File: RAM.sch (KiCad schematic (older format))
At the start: 47 parts, among them U2 AS4C256M16D3LC-12BCN, U3 AS4C256M16D3LC-12BCN

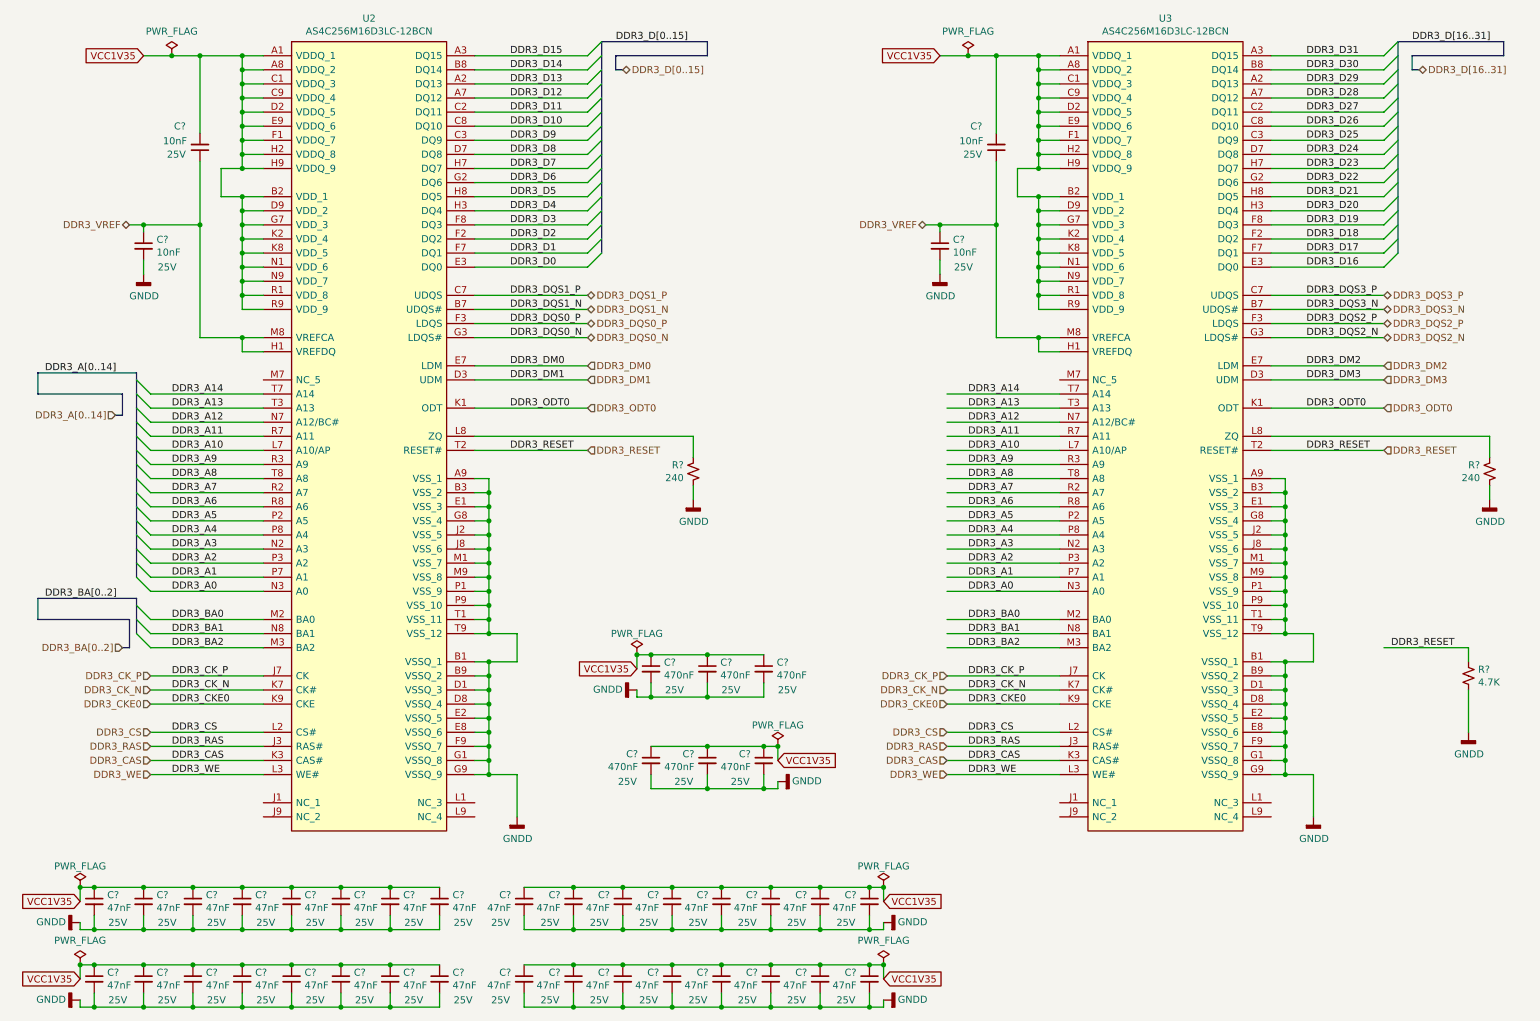
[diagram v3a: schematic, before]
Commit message: PCB created and schematics annotated High speed connections added to the BTB
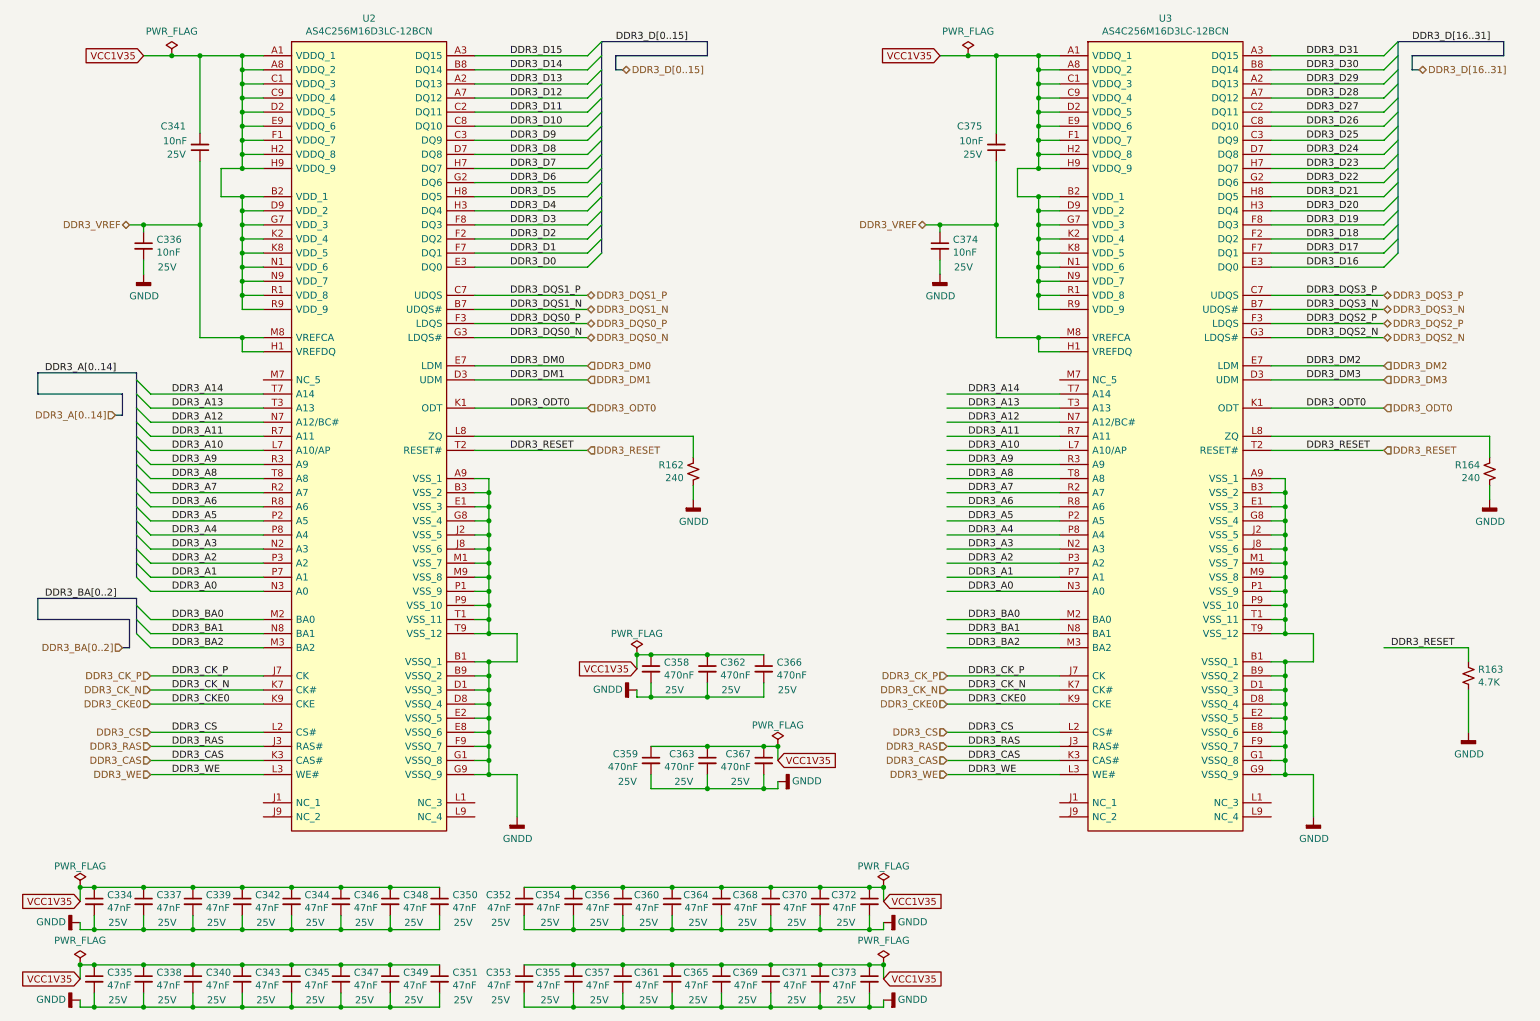
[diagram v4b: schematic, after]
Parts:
- gave numbers to parts that had none: 45

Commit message: Corrected PCB import errors
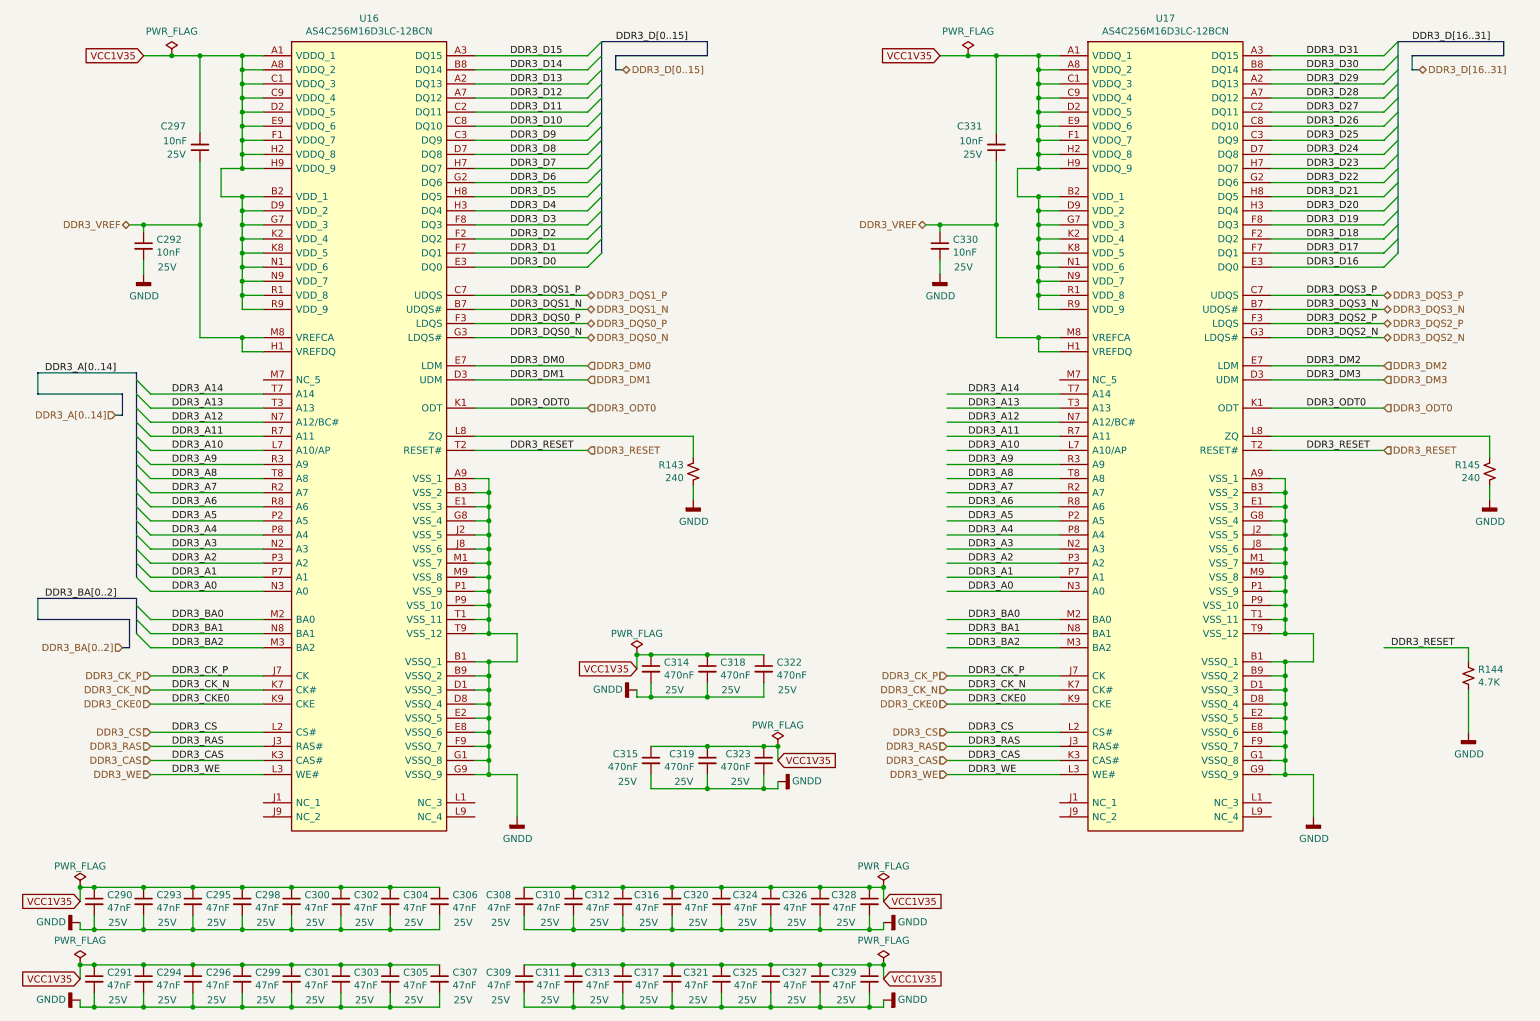
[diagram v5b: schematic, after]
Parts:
- renumbered C334 to C290, C335 to C291, C336 to C292, C337 to C293, C338 to C294, C339 to C295, C340 to C296, C341 to C297, C342 to C298, C343 to C299, C344 to C300, C345 to C301, C346 to C302, C347 to C303, C348 to C304, C349 to C305, C350 to C306, C351 to C307, C352 to C308, C353 to C309, C354 to C310, C355 to C311, C356 to C312, C357 to C313, C358 to C314, C359 to C315, C360 to C316, C361 to C317, C362 to C318, C363 to C319, C364 to C320, C365 to C321, C366 to C322, C367 to C323, C368 to C324, C369 to C325, C370 to C326, C371 to C327, C372 to C328, C373 to C329, C374 to C330, C375 to C331, R162 to R143, R163 to R144, R164 to R145, U2 to U16, U3 to U17
